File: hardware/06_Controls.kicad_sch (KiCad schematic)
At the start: 55 parts, among them J4 BUTTON+LED, J8 FRONTLIGHT 6p, Q5 BC857B, Q6 2N7002K, Q7 2N7002K, SW3 DIAG, U18 BCR421UW6, U19 AL8861QMP-13

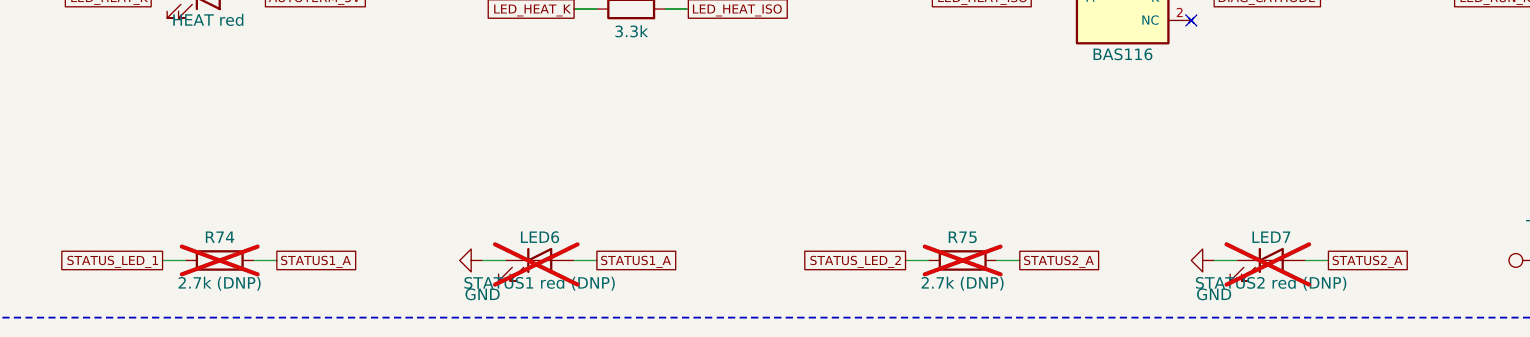
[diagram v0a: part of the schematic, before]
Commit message: Place Rev A board: 4-layer stackup, zones, two-sided placement
Generated by scripts/rebuild/gen_pcb.py from the same circuit definition.
Pre-route DRC: 0 errors, schematic parity: 0 issues.

Co-Authored-By: Claude Opus 5.5 <noreply@anthropic.com>
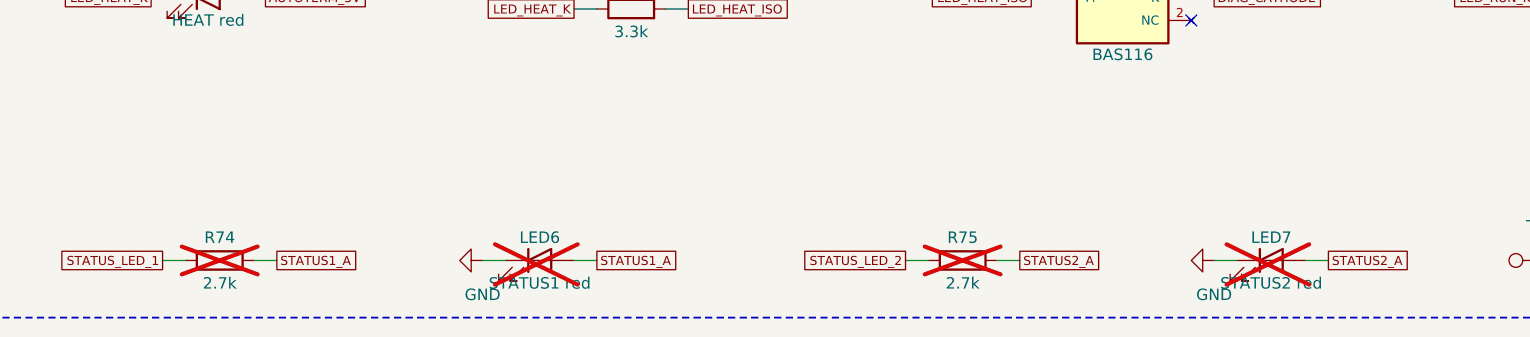
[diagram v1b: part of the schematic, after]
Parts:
- LED6: value STATUS1 red (DNP) -> STATUS1 red
- LED7: value STATUS2 red (DNP) -> STATUS2 red
- R74, R75: value 2.7k (DNP) -> 2.7k
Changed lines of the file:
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@@
 			)
 		)
-		(property "Value" "2.7k (DNP)"
+		(property "Value" "2.7k"
 			(at 40.64 243.84 270)
 			(effects
@@
 			)
 		)
-		(property "Value" "STATUS1 red (DNP)"
+		(property "Value" "STATUS1 red"
 			(at 76.2 243.84 0)
 			(effects
@@
 			)
 		)
-		(property "Value" "2.7k (DNP)"
+		(property "Value" "2.7k"
 			(at 123.19 243.84 270)
 			(effects
@@
 			)
 		)
-		(property "Value" "STATUS2 red (DNP)"
+		(property "Value" "STATUS2 red"
 			(at 157.48 243.84 0)
 			(effects
